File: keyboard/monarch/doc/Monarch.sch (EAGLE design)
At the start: 186 parts, among them J1 MINIUSB, U2 ATMEGA32U4, Y1 16MHZ

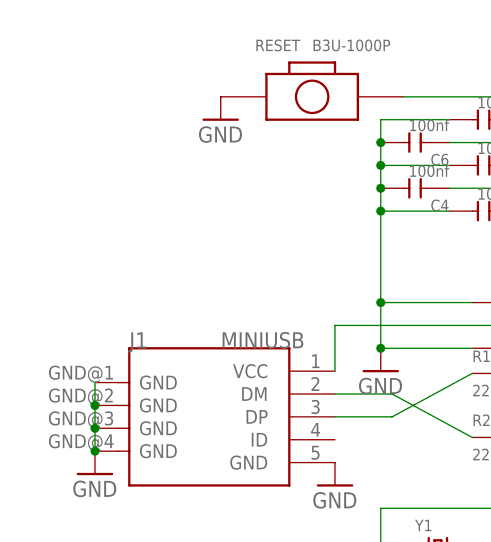
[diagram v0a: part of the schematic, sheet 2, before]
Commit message: Update the Monarch docs to revision 10 of the board
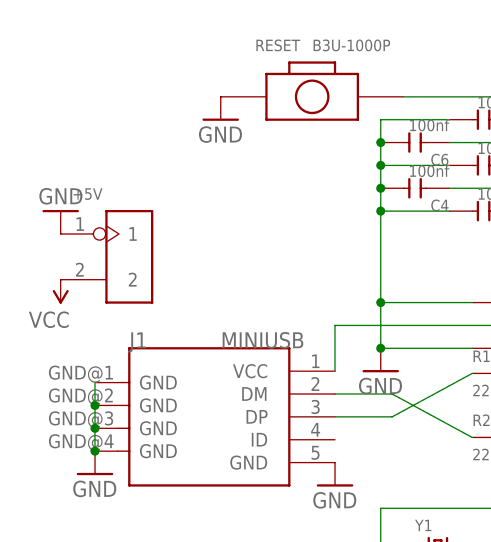
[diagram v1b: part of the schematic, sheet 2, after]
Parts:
- added +5V: (no value), Seeed-OPL-Connector:DIP-BLACK-FEMALE-HEADER-VERT(2P-2.54)
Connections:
- net GND: now also +5V.1
- net VCC: now also +5V.2
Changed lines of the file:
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@@
 <part name="GND9" library="SparkFun-Aesthetics" deviceset="GND" device=""/>
 <part name="SUPPLY2" library="SparkFun-Aesthetics" deviceset="VCC" device=""/>
+<part name="+5V" library="Seeed-OPL-Connector" deviceset="DIP-BLACK-FEMALE-HEADER-VERT(2P-2.54)" device=""/>
+<part name="SUPPLY3" library="SparkFun-Aesthetics" deviceset="VCC" device=""/>
+<part name="GND3" library="SparkFun-Aesthetics" deviceset="GND" device=""/>
 </parts>
 <sheets>
@@
 <instance part="GND9" gate="1" x="73.66" y="55.88"/>
 <instance part="SUPPLY2" gate="G$1" x="91.44" y="63.5"/>
+<instance part="+5V" gate="G$1" x="45.72" y="68.58"/>
+<instance part="SUPPLY3" gate="G$1" x="38.1" y="66.04" rot="R180"/>
+<instance part="GND3" gate="1" x="38.1" y="73.66" rot="R180"/>
 </instances>
 <busses>
@@
 <junction x="41.91" y="46.99"/>
 </segment>
+<segment>
+<pinref part="+5V" gate="G$1" pin="1"/>
+<pinref part="GND3" gate="1" pin="GND"/>
+</segment>
 </net>
 <net name="N$77" class="0">
@@
 <pinref part="SUPPLY2" gate="G$1" pin="VCC"/>
 </segment>
-</net>
+<segment>
+<pinref part="+5V" gate="G$1" pin="2"/>
+<pinref part="SUPPLY3" gate="G$1" pin="VCC"/>
+</segment>
+</net>

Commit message: Updating the monarch design files
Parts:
- removed +5V: (no value), Seeed-OPL-Connector:DIP-BLACK-FEMALE-HEADER-VERT(2P-2.54)
- added FET5: MOSFET, smd-ipc:MOSFET
- added J2: 3p-2.54, Seeed-OPL-Connector:DIP-BLACK-FEMALE-HEADER-VERT(3P-2.54)
- added J3: (no value), Seeed-OPL-Connector:DIP-BLACK-FEMALE-HEADER-VERT(2P-2.54)
- added J4: 5p-2.54, Seeed-OPL-Connector:DIP-BLACK-MALE-HEADER-VERT(4P-2.54)
- added LED1, LED10, LED11, LED12, LED13, LED14, LED15, LED16, LED2, LED3, LED4, LED5, LED6, LED7, LED8, LED9: SMD-LED-GENERIC, AlpsCherry:SMD-LED-GENERIC
- added R10, R11, R12, R13, R14, R15, R16, R17, R18, R19, R5, R6, R7, R8, R9: 100R, Seeed-OPL-Resistor:SMD-RES-100R-5%-1/8W(0805)
- added R20: 10K, Seeed-OPL-Resistor:SMD-RES-10K-1%-1/8W(0805)
- added R4: (no value), Seeed-OPL-Resistor:SMD-RES-100R-5%-1/8W(0805)
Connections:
- new net LED1: J4.P$3, U2.PB6(PCINT6/OC1B/OC4B/ADC13)
- new net LED2: J4.P$2, U2.PC6(OC3A/!OC4A)
- new net N$100: LED11.MINUS, R14.2
- new net N$101: LED10.MINUS, R13.2
- new net N$102: LED9.MINUS, R12.2
- new net N$103: LED8.MINUS, R11.2
- new net N$104: LED7.MINUS, R10.2
- new net N$105: LED14.MINUS, R17.2
- new net N$106: LED13.MINUS, R16.2
- new net N$154: FET5.GATE, J2.P$1, J3.1, R20.2
- new net N$91: LED1.MINUS, R4.2
- new net N$92: LED2.MINUS, R5.2
- new net N$93: LED3.MINUS, R6.2
- new net N$94: LED4.MINUS, R7.2
- new net N$95: LED5.MINUS, R8.2
- new net N$96: LED6.MINUS, R9.2
- new net N$97: LED15.MINUS, R18.2
- new net N$98: LED16.MINUS, R19.2
- new net N$99: LED12.MINUS, R15.2
- new net UNDERLIGHT: FET5.DRAIN, J3.2, R10.1, R11.1, R12.1, R13.1, R14.1, R15.1, R16.1, R17.1, R18.1, R19.1, R4.1, R5.1, R6.1, R7.1, R8.1, R9.1
- net GND: now also FET5.SOURCE, J4.P$1, R20.1; no longer +5V.1
- net N$86: now also J2.P$2; no longer U2.PB6(PCINT6/OC1B/OC4B/ADC13)
- net N$90: now also J2.P$3; no longer U2.PC6(OC3A/!OC4A)
- net VCC: now also J4.P$4, LED1.PLUS, LED10.PLUS, LED11.PLUS, LED12.PLUS, LED13.PLUS, LED14.PLUS, LED15.PLUS, LED16.PLUS, LED2.PLUS, LED3.PLUS, LED4.PLUS, LED5.PLUS, LED6.PLUS, LED7.PLUS, LED8.PLUS, LED9.PLUS; no longer +5V.2
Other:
- moved on the sheet: RLCAPSLOCK, RLCLEAR

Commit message: Update the monarch schematic and layout
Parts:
- removed J1: MINIUSB, Seeed-OPL-Connector:MINI-USB2.0-RECEPT-5POS-4-LEGS-(ST-USB-013A)
- added X1: MINI-USB-UX60-MB-5S8, con-hirose:MINI-USB-UX60-MB-5S8
- renumbered FET5 to FET1, RCMD1 to RCMD, U2 to U1
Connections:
- net GND: now also X1.5; no longer J1.GND@1, J1.GND@2, J1.GND@3, J1.GND@4, J1.GND@5
- net N$88: now also X1.3; no longer J1.DP
- net N$89: now also X1.2; no longer J1.DM
- net VCC: now also X1.1; no longer J1.VCC
